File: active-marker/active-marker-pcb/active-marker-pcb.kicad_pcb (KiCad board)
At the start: 2 copper layers, 45 x 35 mm, 44 parts, among them J1 Conn_01x10, J13 Conn_01x04, J2 Conn_01x04, J3 Conn_01x04, J4 Conn_01x04, J5 Conn_01x04, J6 Conn_01x04, J7 Conn_01x04, SW1 SW_DIP_x02, SW2 SW_Push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

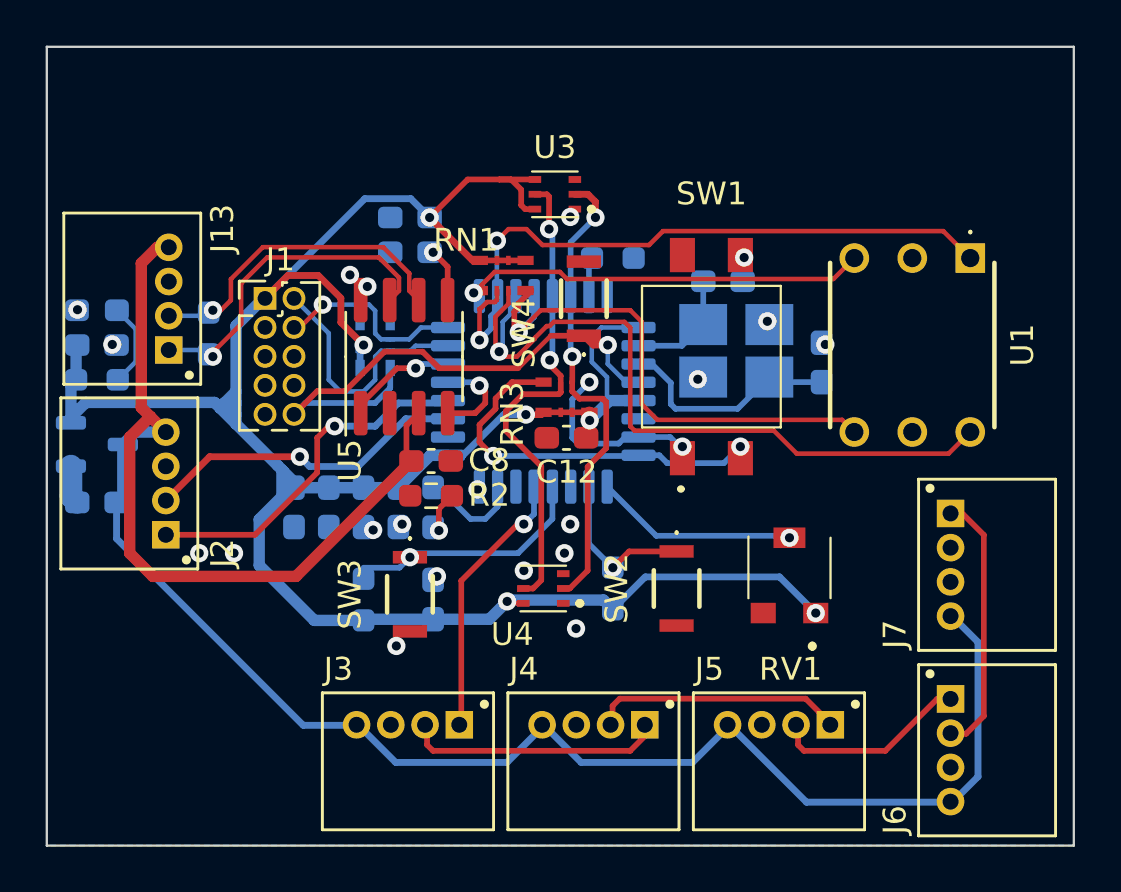
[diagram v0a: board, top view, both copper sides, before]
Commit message: fix Pinmap and add some vias
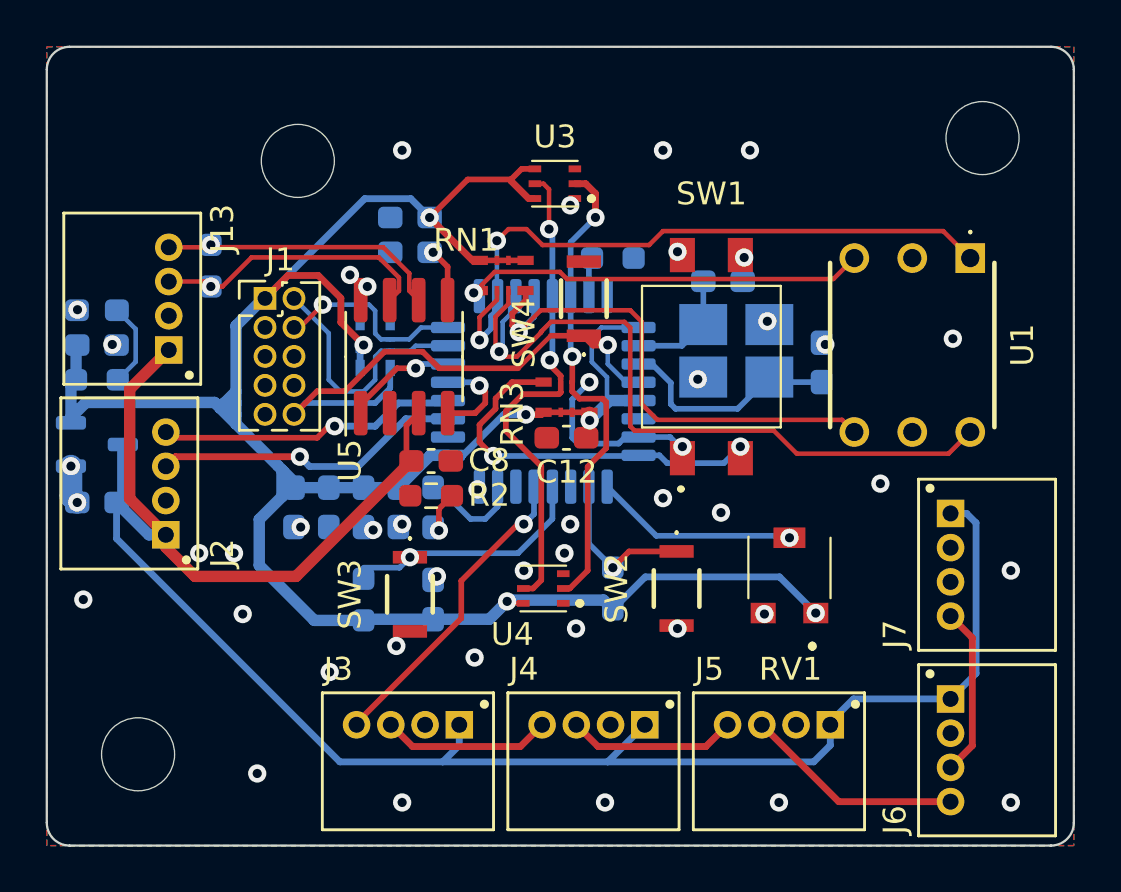
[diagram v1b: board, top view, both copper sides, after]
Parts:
- added H1: MountingHole, MountingHole:MountingHole_3.2mm_M3_ISO7380, F.Cu at (104.0, 116.0)
- added H2: MountingHole, MountingHole:MountingHole_3.2mm_M3_ISO7380, F.Cu at (141.0, 89.0)
- added H3: MountingHole, MountingHole:MountingHole_3.2mm_M3_ISO7380, F.Cu at (111.0, 90.0)
- moved R3 2.97 mm to (107.2, 94.6)
- moved U3 0.46 mm to (122.3, 91.0)
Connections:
- J13 pad 1: /CAN+ -> /CAN-
- J13 pad 2: /CAN- -> /CAN+
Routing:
- net /D45: track 11.4 -> 7.42 mm
- net /D12: track 11.3 -> 7.42 mm
- net /D23: track 11.1 -> 7.42 mm
- net +5V: track 92.4 -> 88.7 mm
- net /UART_RX: track 15.7 -> 13.1 mm
- net /CAN+: track 14.5 -> 12.2 mm
- net /SPI_MOSI: track 11.9 -> 13.8 mm
- net /CAN-: track 13.9 -> 12.4 mm
- net /D34: track 8.65 -> 9.66 mm
- net +3V3: track 110.3 -> 109.5 mm
- net /UART_TX: track 14.2 -> 13.6 mm
- net GND: vias 20 -> 43
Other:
- outline, holes or cut-outs redrawn
